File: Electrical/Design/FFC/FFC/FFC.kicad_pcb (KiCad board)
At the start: 2 copper layers, 13 x 15 mm, 4 parts, among them J1 Conn_01x08, J2 Conn_01x08

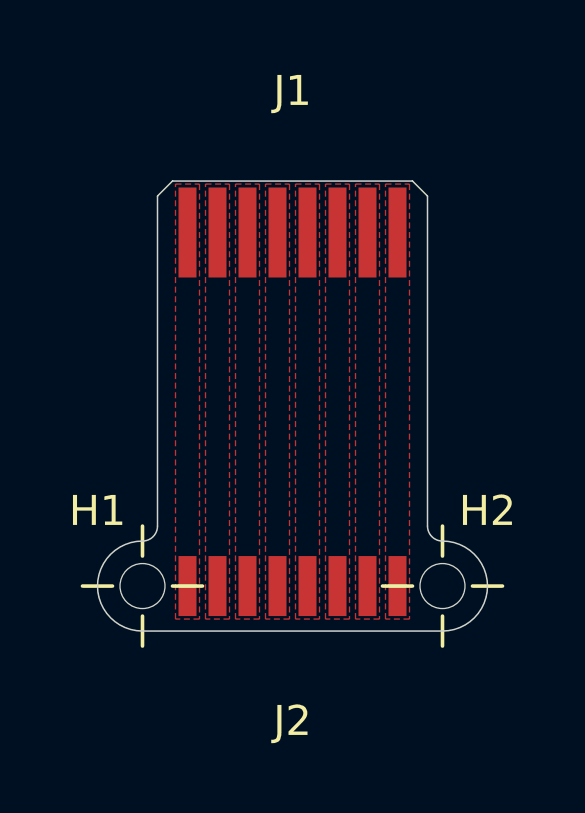
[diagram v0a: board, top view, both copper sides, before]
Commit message: SUKU FFC stiffner location fixed + GERBER
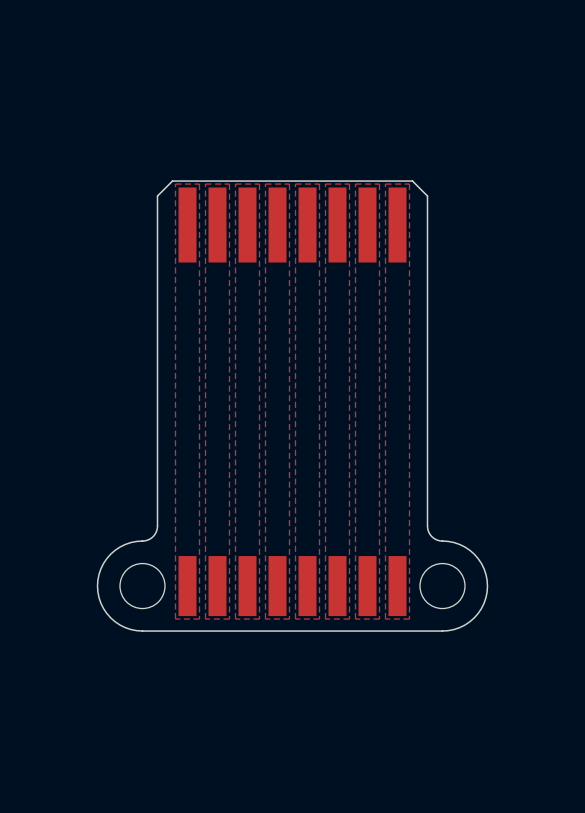
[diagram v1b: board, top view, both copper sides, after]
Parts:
- H1, H2: moved to B.Cu
- moved J1 0.25 mm to (100.0, 86.5)
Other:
- board text added: "2020/2"
- board text added: "PI STIFFENER TO FFC CONNECTOR"
- board text removed: "STIFFENER TO FFC CONNECTOR"

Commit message: SUKU updated FFC with combined2 FFC footprint
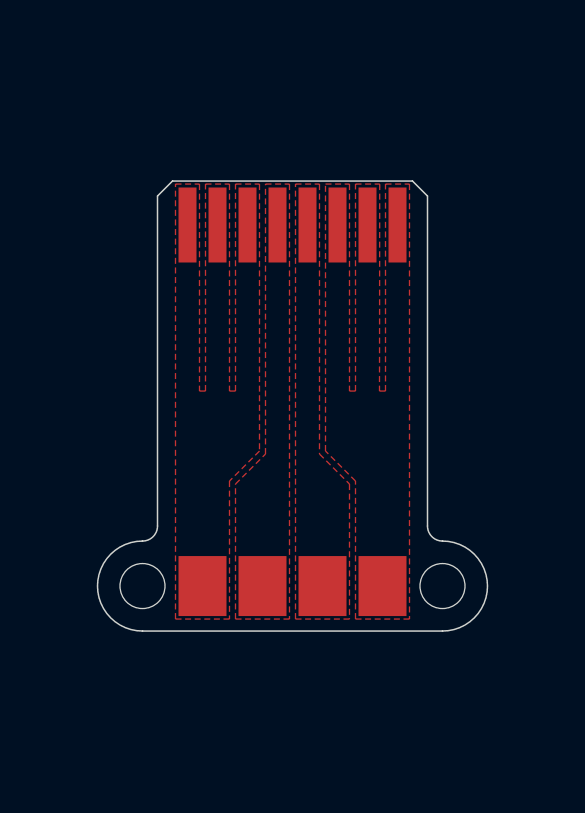
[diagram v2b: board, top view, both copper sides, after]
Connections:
- J1 pad 2: Net-(J1-Pad2) -> Net-(J1-Pad1)
- J1 pad 3: Net-(J1-Pad3) -> Net-(J1-Pad1)
- J1 pad 7: Net-(J1-Pad7) -> Net-(J1-Pad6)
- J1 pad 8: Net-(J1-Pad8) -> Net-(J1-Pad6)
- J2 pad 8: Net-(J1-Pad8) -> Net-(J1-Pad6)
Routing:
- removed copper zone on F.Cu, net Net-(J1-Pad2)
- removed copper zone on F.Cu, net Net-(J1-Pad3)
- removed copper zone on F.Cu, net Net-(J1-Pad7)
- removed copper zone on F.Cu, net Net-(J1-Pad8)
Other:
- board text added: "2020/4"
- board text removed: "2020/2"
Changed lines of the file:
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@@
   (general
     (thickness 0.1)
-    (drawings 28)
+    (drawings 32)
     (tracks 0)
     (zones 0)
     (modules 4)
-    (nets 9)
+    (nets 5)
   )
   (page A4)
@@
   )
   (net 0 "")
-  (net 1 "Net-(J1-Pad8)")
-  (net 2 "Net-(J1-Pad6)")
-  (net 3 "Net-(J1-Pad4)")
-  (net 4 "Net-(J1-Pad2)")
-  (net 5 "Net-(J1-Pad7)")
-  (net 6 "Net-(J1-Pad5)")
-  (net 7 "Net-(J1-Pad3)")
-  (net 8 "Net-(J1-Pad1)")
+  (net 1 "Net-(J1-Pad6)")
+  (net 2 "Net-(J1-Pad4)")
+  (net 3 "Net-(J1-Pad5)")
+  (net 4 "Net-(J1-Pad1)")
   (net_class Default "This is the default net class."
     (clearance 0.2)
@@
     (uvia_drill 0.1)
     (add_net "Net-(J1-Pad1)")
-    (add_net "Net-(J1-Pad2)")
-    (add_net "Net-(J1-Pad3)")
     (add_net "Net-(J1-Pad4)")
     (add_net "Net-(J1-Pad5)")
     (add_net "Net-(J1-Pad6)")
-    (add_net "Net-(J1-Pad7)")
-    (add_net "Net-(J1-Pad8)")
   )
   (module suku_basics:J_FFC_1x8_SOLDER_2 (layer F.Cu)
@@
     (fp_line (start 4.5 2.25) (end 4.5 -2.25) (layer F.CrtYd) (width 0.05))
     (fp_line (start -4.5 2.25) (end 4.5 2.25) (layer F.CrtYd) (width 0.05))
-    (pad 8 smd rect (at 3.5 0 90) (size 2 0.6) (layers F.Cu F.Paste F.Mask)
-      (net 1 "Net-(J1-Pad8)"))
-    (pad 6 smd rect (at 1.5 0 90) (size 2 0.6) (layers F.Cu F.Paste F.Mask)
-      (net 2 "Net-(J1-Pad6)"))
-    (pad 4 smd rect (at -0.5 0 90) (size 2 0.6) (layers F.Cu F.Paste F.Mask)
-      (net 3 "Net-(J1-Pad4)"))
-    (pad 2 smd rect (at -2.5 0 90) (size 2 0.6) (layers F.Cu F.Paste F.Mask)
-      (net 4 "Net-(J1-Pad2)"))
-    (pad 7 smd rect (at 2.5 0 90) (size 2 0.6) (layers F.Cu F.Paste F.Mask)
-      (net 5 "Net-(J1-Pad7)"))
-    (pad 5 smd rect (at 0.5 0 90) (size 2 0.6) (layers F.Cu F.Paste F.Mask)
-      (net 6 "Net-(J1-Pad5)"))
-    (pad 3 smd rect (at -1.5 0 90) (size 2 0.6) (layers F.Cu F.Paste F.Mask)
-      (net 7 "Net-(J1-Pad3)"))
-    (pad 1 smd rect (at -3.5 0 90) (size 2 0.6) (layers F.Cu F.Paste F.Mask)
-      (net 8 "Net-(J1-Pad1)"))
+    (pad 8 smd rect (at 3 0 90) (size 2 1.6) (layers F.Cu F.Paste F.Mask)
+      (net 1 "Net-(J1-Pad6)"))
+    (pad 4 smd rect (at -1 0 90) (size 2 1.6) (layers F.Cu F.Paste F.Mask)
+      (net 2 "Net-(J1-Pad4)"))
+    (pad 5 smd rect (at 1 0 90) (size 2 1.6) (layers F.Cu F.Paste F.Mask)
+      (net 3 "Net-(J1-Pad5)"))
+    (pad 1 smd rect (at -3 0 90) (size 2 1.6) (layers F.Cu F.Paste F.Mask)
+      (net 4 "Net-(J1-Pad1)"))
   )
   (module suku_basics:J_FFC_1x8_STIFFENER (layer F.Cu)
@@
     (fp_line (start -4.5 2.25) (end 4.5 2.25) (layer F.CrtYd) (width 0.05))
     (pad 8 smd rect (at 3.5 0 90) (size 2.5 0.6) (layers F.Cu F.Paste F.Mask)
-      (net 1 "Net-(J1-Pad8)"))
+      (net 1 "Net-(J1-Pad6)"))
     (pad 6 smd rect (at 1.5 0 90) (size 2.5 0.6) (layers F.Cu F.Paste F.Mask)
-      (net 2 "Net-(J1-Pad6)"))
+      (net 1 "Net-(J1-Pad6)"))
     (pad 4 smd rect (at -0.5 0 90) (size 2.5 0.6) (layers F.Cu F.Paste F.Mask)
-      (net 3 "Net-(J1-Pad4)"))
+      (net 2 "Net-(J1-Pad4)"))
     (pad 2 smd rect (at -2.5 0 90) (size 2.5 0.6) (layers F.Cu F.Paste F.Mask)
-      (net 4 "Net-(J1-Pad2)"))
+      (net 4 "Net-(J1-Pad1)"))
     (pad 7 smd rect (at 2.5 0 90) (size 2.5 0.6) (layers F.Cu F.Paste F.Mask)
-      (net 5 "Net-(J1-Pad7)"))
+      (net 1 "Net-(J1-Pad6)"))
     (pad 5 smd rect (at 0.5 0 90) (size 2.5 0.6) (layers F.Cu F.Paste F.Mask)
-      (net 6 "Net-(J1-Pad5)"))
+      (net 3 "Net-(J1-Pad5)"))
     (pad 3 smd rect (at -1.5 0 90) (size 2.5 0.6) (layers F.Cu F.Paste F.Mask)
-      (net 7 "Net-(J1-Pad3)"))
+      (net 4 "Net-(J1-Pad1)"))
     (pad 1 smd rect (at -3.5 0 90) (size 2.5 0.6) (layers F.Cu F.Paste F.Mask)
-      (net 8 "Net-(J1-Pad1)"))
+      (net 4 "Net-(J1-Pad1)"))
   )
   (module suku_basics:J_FFC_1.5mm_ALIGNMENT (layer B.Cu)
@@
     (pad "" np_thru_hole circle (at 0 0) (size 1.5 1.5) (drill 1.5) (layers *.Cu *.Mask))
   )
+  (gr_circle (center 97 95.5) (end 97.25 95.5) (layer F.Mask) (width 0.5))
+  (gr_circle (center 99 95.5) (end 99.25 95.5) (layer F.Mask) (width 0.5))
+  (gr_circle (center 101 95.5) (end 101.25 95.5) (layer F.Mask) (width 0.5))
+  (gr_circle (center 103 95.5) (end 103.25 95.5) (layer F.Mask) (width 0.5))
   (gr_line (start 96.5 94.5) (end 96.5 92.5) (layer B.SilkS) (width 0.12))
   (gr_line (start 103.5 94.5) (end 96.5 94.5) (layer B.SilkS) (width 0.12))
   (gr_line (start 103.5 92.5) (end 103.5 94.5) (layer B.SilkS) (width 0.12))
   (gr_line (start 96.5 92.5) (end 103.5 92.5) (layer B.SilkS) (width 0.12))
-  (gr_text 2020/2 (at 100 93.5) (layer B.SilkS)
+  (gr_text 2020/4 (at 100 93.5) (layer B.SilkS)
     (effects (font (size 1 1) (thickness 0.15)) (justify mirror))
   )
@@
   (gr_line (start 95.5 85.5) (end 95.5 96.5) (layer Edge.Cuts) (width 0.05))
   (gr_line (start 96 85) (end 104 85) (layer Edge.Cuts) (width 0.05))
-  (zone (net 8) (net_name "Net-(J1-Pad1)") (layer F.Cu) (hatch edge 0.508)
-    (connect_pads thru_hole_only (clearance 0.255))
-    (min_thickness 0.254)
-    (fill yes (arc_segments 32) (thermal_gap 1) (thermal_bridge_width 0.508))
-    (polygon
-      (pts
-        (xy 96.1 85.2) (xy 96.1 85.1) (xy 96.9 85.1) (xy 96.9 99.6) (xy 96.1 99.6)
-      )
-    )
-  )
-  (zone (net 4) (net_name "Net-(J1-Pad2)") (layer F.Cu) (hatch edge 0.508)
-    (connect_pads thru_hole_only (clearance 0.255))
-    (min_thickness 0.254)
-    (fill yes (arc_segments 32) (thermal_gap 1) (thermal_bridge_width 0.508))
-    (polygon
-      (pts
-        (xy 97.1 85.1) (xy 97.9 85.1) (xy 97.9 99.6) (xy 97.1 99.6)
-      )
-    )
-  )
-  (zone (net 7) (net_name "Net-(J1-Pad3)") (layer F.Cu) (hatch edge 0.508)
-    (connect_pads thru_hole_only (clearance 0.255))
-    (min_thickness 0.254)
-    (fill yes (arc_segments 32) (thermal_gap 1) (thermal_bridge_width 0.508))
-    (polygon
-      (pts
-        (xy 98.1 85.1) (xy 98.9 85.1) (xy 98.9 99.6) (xy 98.1 99.6)
-      )
-    )
-  )
-  (zone (net 3) (net_name "Net-(J1-Pad4)") (layer F.Cu) (hatch edge 0.508)
-    (connect_pads thru_hole_only (clearance 0.255))
-    (min_thickness 0.254)
-    (fill yes (arc_segments 32) (thermal_gap 1) (thermal_bridge_width 0.508))
-    (polygon
-      (pts
-        (xy 99.1 85.1) (xy 99.9 85.1) (xy 99.9 99.6) (xy 99.1 99.6)
-      )
-    )
-  )
-  (zone (net 6) (net_name "Net-(J1-Pad5)") (layer F.Cu) (hatch edge 0.508)
-    (connect_pads thru_hole_only (clearance 0.255))
-    (min_thickness 0.254)
-    (fill yes (arc_segments 32) (thermal_gap 1) (thermal_bridge_width 0.508))
-    (polygon
-      (pts
-        (xy 100.1 85.1) (xy 100.9 85.1) (xy 100.9 99.6) (xy 100.1 99.6)
-      )
-    )
-  )
-  (zone (net 2) (net_name "Net-(J1-Pad6)") (layer F.Cu) (hatch edge 0.508)
-    (connect_pads thru_hole_only (clearance 0.255))
-    (min_thickness 0.254)
-    (fill yes (arc_segments 32) (thermal_gap 1) (thermal_bridge_width 0.508))
-    (polygon
-      (pts
-        (xy 101.1 85.1) (xy 101.9 85.1) (xy 101.9 99.6) (xy 101.1 99.6)
-      )
-    )
-  )
-  (zone (net 5) (net_name "Net-(J1-Pad7)") (layer F.Cu) (hatch edge 0.508)
-    (connect_pads thru_hole_only (clearance 0.255))
-    (min_thickness 0.254)
-    (fill yes (arc_segments 32) (thermal_gap 1) (thermal_bridge_width 0.508))
-    (polygon
-      (pts
-        (xy 102.1 85.1) (xy 102.9 85.1) (xy 102.9 99.6) (xy 102.1 99.6)
-      )
-    )
-  )
-  (zone (net 1) (net_name "Net-(J1-Pad8)") (layer F.Cu) (hatch edge 0.508)
-    (connect_pads thru_hole_only (clearance 0.255))
-    (min_thickness 0.254)
-    (fill yes (arc_segments 32) (thermal_gap 1) (thermal_bridge_width 0.508))
-    (polygon
-      (pts
-        (xy 103.1 85.1) (xy 103.9 85.1) (xy 103.9 99.6) (xy 103.1 99.6)
-      )
-    )
+  (zone (net 4) (net_name "Net-(J1-Pad1)") (layer F.Cu) (hatch edge 0.508)
+    (connect_pads thru_hole_only (clearance 0.255))
+    (min_thickness 0.254)
+    (fill yes (arc_segments 32) (thermal_gap 1) (thermal_bridge_width 0.508))
+    (polygon
+      (pts
+        (xy 98.1 85.1) (xy 98.9 85.1) (xy 98.9 94) (xy 97.9 95) (xy 97.9 99.6)
+        (xy 96.1 99.6) (xy 96.1 85.1) (xy 96.9 85.1) (xy 96.9 92) (xy 97.1 92)
+        (xy 97.1 85.1) (xy 97.9 85.1) (xy 97.9 92) (xy 98.1 92)
+      )
+    )
+  )
+  (zone (net 2) (net_name "Net-(J1-Pad4)") (layer F.Cu) (hatch edge 0.508)
+    (connect_pads thru_hole_only (clearance 0.255))
+    (min_thickness 0.254)
+    (fill yes (arc_segments 32) (thermal_gap 1) (thermal_bridge_width 0.508))
+    (polygon
+      (pts
+        (xy 98.1 95.1) (xy 99.1 94.1) (xy 99.1 85.1) (xy 99.9 85.1) (xy 99.9 99.6)
+        (xy 98.1 99.6)
+      )
+    )
+  )
+  (zone (net 3) (net_name "Net-(J1-Pad5)") (layer F.Cu) (hatch edge 0.508)
+    (connect_pads thru_hole_only (clearance 0.255))
+    (min_thickness 0.254)
+    (fill yes (arc_segments 32) (thermal_gap 1) (thermal_bridge_width 0.508))
+    (polygon
+      (pts
+        (xy 100.1 85.1) (xy 100.9 85.1) (xy 100.9 94.1) (xy 101.9 95.1) (xy 101.9 99.6)
+        (xy 100.1 99.6)
+      )
+    )
+  )
+  (zone (net 1) (net_name "Net-(J1-Pad6)") (layer F.Cu) (hatch edge 0.508)
+    (connect_pads thru_hole_only (clearance 0.255))
+    (min_thickness 0.254)
+    (fill yes (arc_segments 32) (thermal_gap 1) (thermal_bridge_width 0.508))
+    (polygon
+      (pts
+        (xy 102.1 95) (xy 101.1 94) (xy 101.1 85.1) (xy 101.9 85.1) (xy 101.9 92)
+        (xy 102.1 92) (xy 102.1 85.1) (xy 102.90789 85.1) (xy 102.9 92) (xy 103.1 92)
+        (xy 103.1 85.1) (xy 103.9 85.1) (xy 103.9 99.6) (xy 102.1 99.6)
+      )
+    )
